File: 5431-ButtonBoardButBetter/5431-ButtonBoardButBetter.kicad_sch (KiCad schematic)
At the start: 21 parts, among them SW1 SW_DIP_x01, SW10 SW_DIP_x01, SW11 SW_DIP_x01, SW12 SW_DIP_x01, SW13 SW_DIP_x01, SW14 SW_DIP_x01, SW15 SW_DIP_x01, SW16 SW_DIP_x01, SW17 SW_DIP_x01, SW2 SW_DIP_x01, SW3 SW_DIP_x01, SW5 SW_DIP_x01, SW6 SW_DIP_x01, SW7 SW_DIP_x01, SW8 SW_DIP_x01, U1 Pico, U2 MCP3008, U3 COM-09032, U4 COM-09032

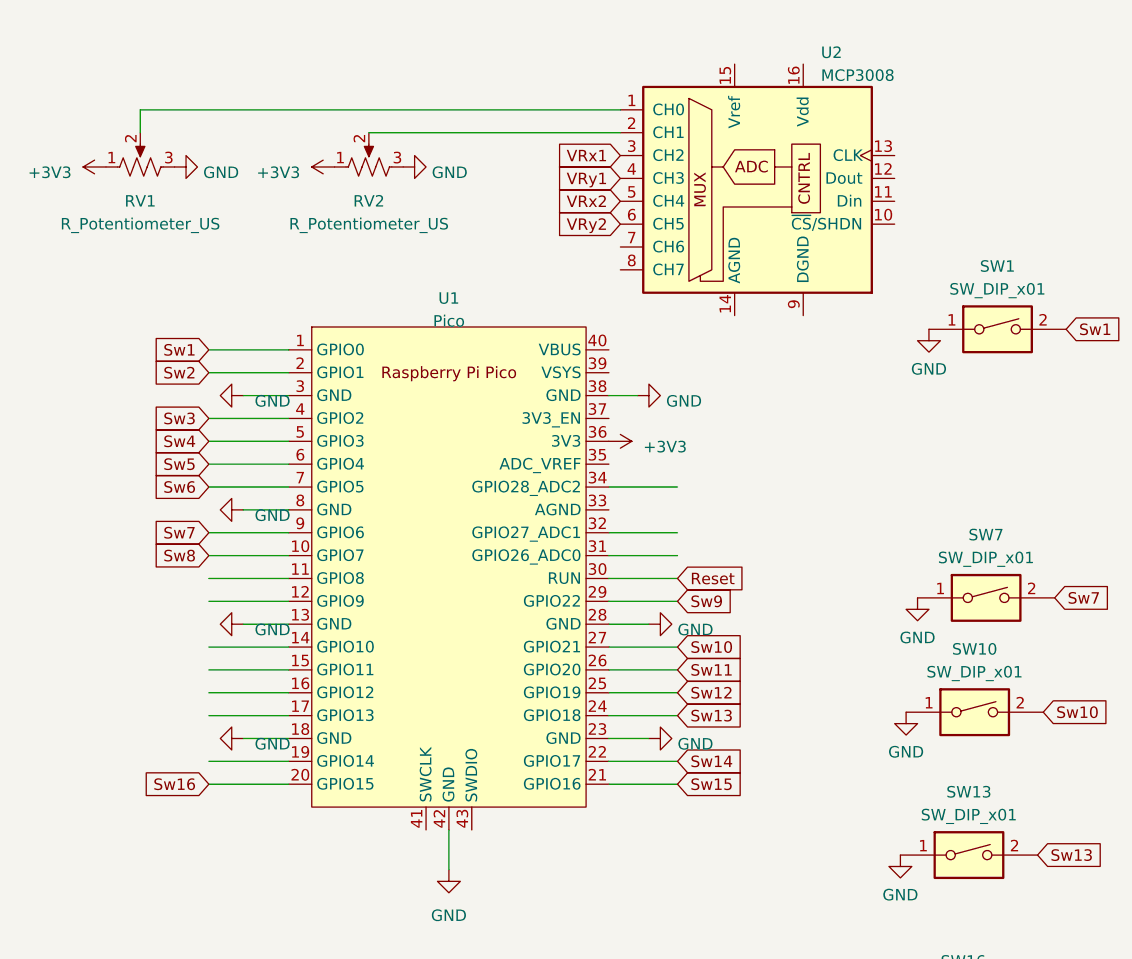
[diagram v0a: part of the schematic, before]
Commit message: linked mux to pico
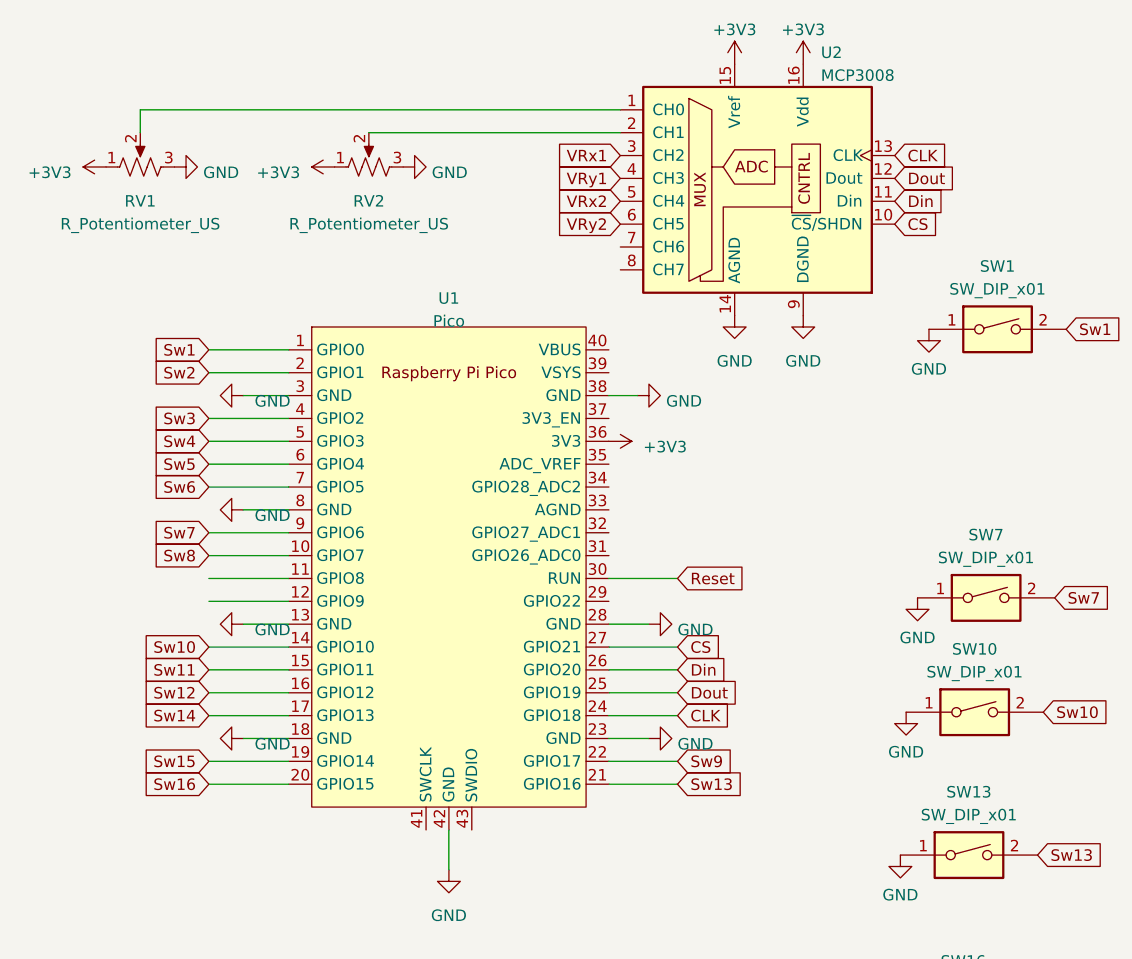
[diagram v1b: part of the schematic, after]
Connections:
- net +3V3: now also U2.15 (Vref), U2.16 (Vdd)
- net GND: now also U2.14 (AGND), U2.9 (DGND)
- net Sw10: now also U1.14 (GPIO10); no longer U1.27 (GPIO21)
- net Sw11: now also U1.15 (GPIO11); no longer U1.26 (GPIO20)
- net Sw12: now also U1.16 (GPIO12); no longer U1.25 (GPIO19)
- net Sw13: now also U1.21 (GPIO16); no longer U1.24 (GPIO18)
- net Sw14: now also U1.17 (GPIO13); no longer U1.22 (GPIO17)
- net Sw15: now also U1.19 (GPIO14); no longer U1.21 (GPIO16)
- net Sw9: now also U1.22 (GPIO17); no longer U1.29 (GPIO22)
- net CS: now reaches U2.10 (~{CS}/SHDN)
- net CS: now also U1.27 (GPIO21)
- net Din: now reaches U2.11 (Din)
- net Din: now also U1.26 (GPIO20)
- net Dout: now reaches U2.12 (Dout)
- net Dout: now also U1.25 (GPIO19)
- net CLK: now reaches U2.13 (CLK)
- net CLK: now also U1.24 (GPIO18)

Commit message: better IC footprint
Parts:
- U2: footprint Socket:DIP_Socket-16_W4.3_W5.08_W7.62_W10.16_W10.9_3M_216-3340-00-0602J -> Package_DIP:DIP-16_W7.62mm_Socket
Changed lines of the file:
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@@
       (effects (font (size 1.27 1.27)) (justify left))
     )
-    (property "Footprint" "Socket:DIP_Socket-16_W4.3_W5.08_W7.62_W10.16_W10.9_3M_216-3340-00-0602J" (at 127 29.21 0)
+    (property "Footprint" "Package_DIP:DIP-16_W7.62mm_Socket" (at 127 29.21 0)
       (effects (font (size 1.27 1.27)) hide)
     )

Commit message: final layout
edge cuts and traces left
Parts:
- added H1, H2, H3, H4: MountingHole, symbol Mechanical:MountingHole
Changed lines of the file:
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@@
-    (stroke (width 0) (type default))
-  )
-  (wire (pts (xy 63.5 78.74) (xy 72.39 78.74))
     (stroke (width 0) (type default))
   )
@@
   )
   (wire (pts (xy 63.5 99.06) (xy 72.39 99.06))
-    (stroke (width 0) (type default))
-  )
-  (wire (pts (xy 63.5 76.2) (xy 72.39 76.2))
     (stroke (width 0) (type default))
   )
@@
         (path "/85ad268b-acfd-4dd1-a78b-2229ab217983"
           (reference "#PWR039") (unit 1)
+        )
+      )
+    )
+  )
+  (symbol (lib_id "Mechanical:MountingHole") (at 21.59 45.085 0) (unit 1)
+    (in_bom yes) (on_board yes) (dnp no) (fields_autoplaced)
+    (property "Reference" "H4" (at 24.765 44.45 0)
+      (effects (font (size 1.27 1.27)) (justify left))
+    )
+    (property "Value" "MountingHole" (at 24.765 46.99 0)
+      (effects (font (size 1.27 1.27)) (justify left))
+    )
+    (property "Footprint" "" (at 21.59 45.085 0)
+      (effects (font (size 1.27 1.27)) hide)
+    )
+    (property "Datasheet" "~" (at 21.59 45.085 0)
+      (effects (font (size 1.27 1.27)) hide)
+    )
+    (instances
+      (project "5431-ButtonBoardButBetter"
+        (path "/85ad268b-acfd-4dd1-a78b-2229ab217983"
+          (reference "H4") (unit 1)
         )
       )
@@
     )
   )
+  (symbol (lib_id "Mechanical:MountingHole") (at 24.13 55.245 0) (unit 1)
+    (in_bom yes) (on_board yes) (dnp no) (fields_autoplaced)
+    (property "Reference" "H3" (at 27.305 54.61 0)
+      (effects (font (size 1.27 1.27)) (justify left))
+    )
+    (property "Value" "MountingHole" (at 27.305 57.15 0)
+      (effects (font (size 1.27 1.27)) (justify left))
+    )
+    (property "Footprint" "" (at 24.13 55.245 0)
+      (effects (font (size 1.27 1.27)) hide)
+    )
+    (property "Datasheet" "~" (at 24.13 55.245 0)
+      (effects (font (size 1.27 1.27)) hide)
+    )
+    (instances
+      (project "5431-ButtonBoardButBetter"
+        (path "/85ad268b-acfd-4dd1-a78b-2229ab217983"
+          (reference "H3") (unit 1)
+        )
+      )
+    )
+  )
   (symbol (lib_id "power:GND") (at 241.3 64.135 270) (unit 1)
     (in_bom yes) (on_board yes) (dnp no) (fields_autoplaced)
@@
         (path "/85ad268b-acfd-4dd1-a78b-2229ab217983"
           (reference "#PWR011") (unit 1)
+        )
+      )
+    )
+  )
+  (symbol (lib_id "Mechanical:MountingHole") (at 22.86 34.925 0) (unit 1)
+    (in_bom yes) (on_board yes) (dnp no) (fields_autoplaced)
+    (property "Reference" "H2" (at 26.035 34.29 0)
+      (effects (font (size 1.27 1.27)) (justify left))
+    )
+    (property "Value" "MountingHole" (at 26.035 36.83 0)
+      (effects (font (size 1.27 1.27)) (justify left))
+    )
+    (property "Footprint" "" (at 22.86 34.925 0)
+      (effects (font (size 1.27 1.27)) hide)
+    )
+    (property "Datasheet" "~" (at 22.86 34.925 0)
+      (effects (font (size 1.27 1.27)) hide)
+    )
+    (instances
+      (project "5431-ButtonBoardButBetter"
+        (path "/85ad268b-acfd-4dd1-a78b-2229ab217983"
+          (reference "H2") (unit 1)
         )
       )
@@
         )
       )
+    )
+  )
+  (symbol (lib_id "Mechanical:MountingHole") (at 24.765 25.4 0) (unit 1)
+    (in_bom yes) (on_board yes) (dnp no) (fields_autoplaced)
+    (property "Reference" "H1" (at 27.94 24.765 0)
+      (effects (font (size 1.27 1.27)) (justify left))
+    )
+    (property "Value" "MountingHole" (at 27.94 27.305 0)
+      (effects (font (size 1.27 1.27)) (justify left))
+    )
+    (property "Footprint" "" (at 24.765 25.4 0)
+      (effects (font (size 1.27 1.27)) hide)
+    )
+    (property "Datasheet" "~" (at 24.765 25.4 0)
+      (effects (font (size 1.27 1.27)) hide)
+    )
+    (instances
+      (project "5431-ButtonBoardButBetter"
+        (path "/85ad268b-acfd-4dd1-a78b-2229ab217983"
+          (reference "H1") (unit 1)
+        )
+      )
